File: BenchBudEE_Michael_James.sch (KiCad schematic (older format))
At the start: 0 parts

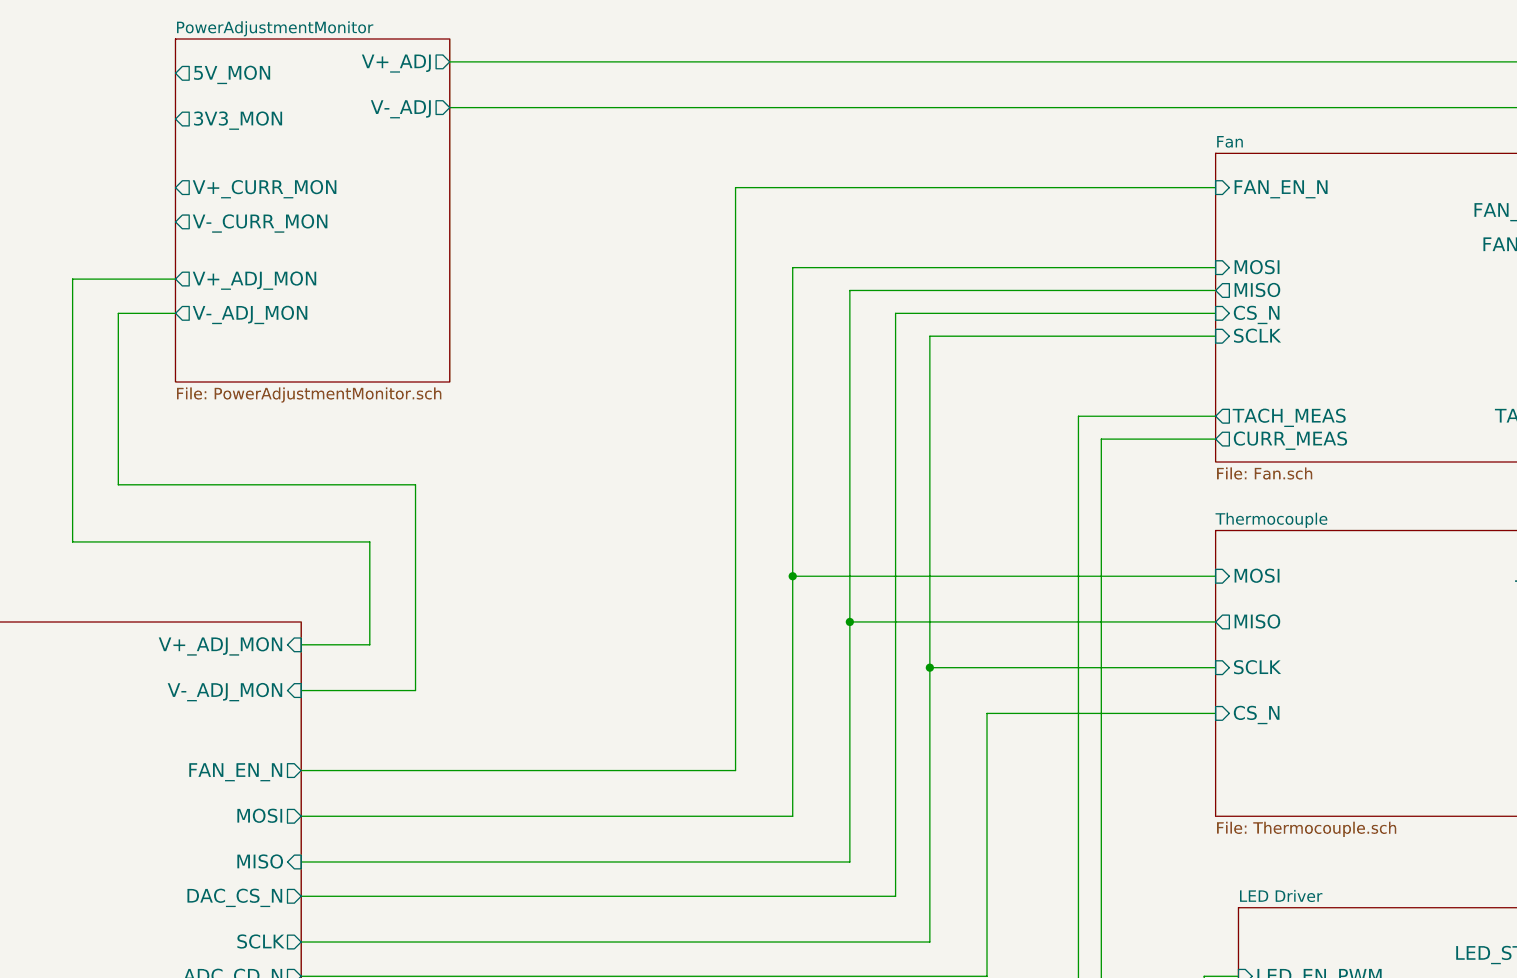
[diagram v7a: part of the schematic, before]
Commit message: M3 U9
Revisiting the Current/Fan Module
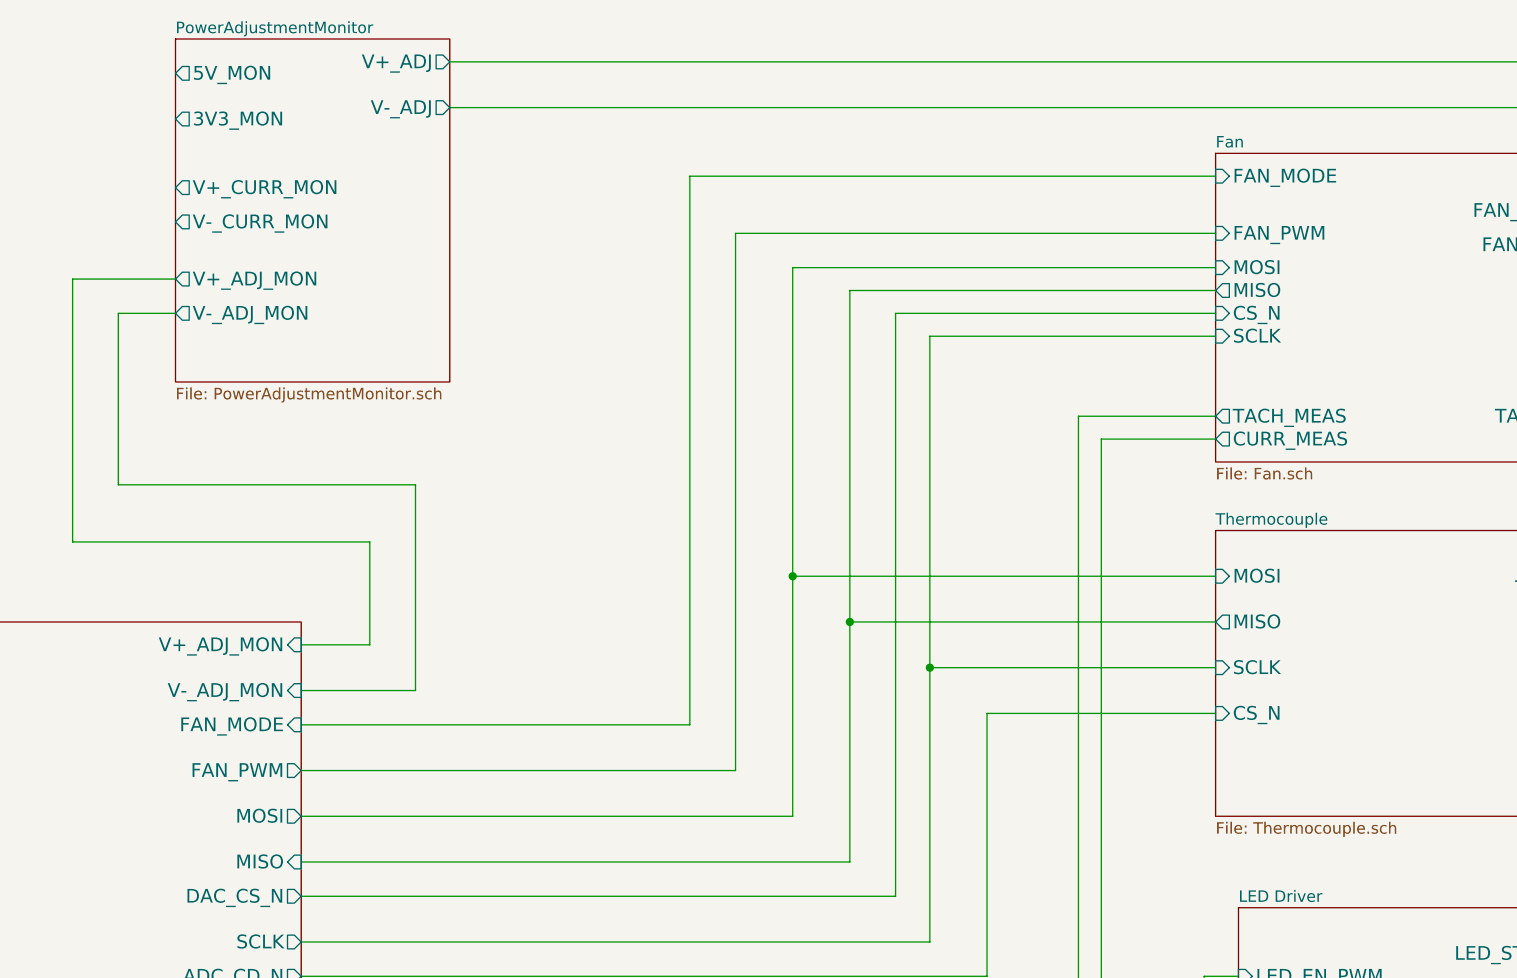
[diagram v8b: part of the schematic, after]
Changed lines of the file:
@@
 F6 "RELAY+" I R 4000 6500 60
 F7 "RELAY-" I R 4000 6800 60
-F8 "FAN_EN_N" O R 4000 3750 60
-F9 "CURR_MEAS" I R 4000 5300 60
-F10 "V+_ADJ_MON" I R 4000 3200 60
-F11 "V-_ADJ_MON" I R 4000 3400 60
-F12 "LED_EN_PWM" I R 4000 4950 60
-F13 "DAC_CS_N" O R 4000 4300 60
-F14 "ADC_CD_N" O R 4000 4650 60
+F8 "CURR_MEAS" I R 4000 5300 60
+F9 "V+_ADJ_MON" I R 4000 3200 60
+F10 "V-_ADJ_MON" I R 4000 3400 60
+F11 "LED_EN_PWM" I R 4000 4950 60
+F12 "DAC_CS_N" O R 4000 4300 60
+F13 "ADC_CD_N" O R 4000 4650 60
+F14 "FAN_PWM" O R 4000 3750 60
+F15 "FAN_MODE" I R 4000 3550 60
 $EndSheet
 $Sheet
@@
 F8 "TACH_IN" I R 9650 2200 60
 F9 "TACH_MEAS" O L 8000 2200 60
-F10 "FAN_EN_N" I L 8000 1200 60
-F11 "CURR_MEAS" O L 8000 2300 60
+F10 "CURR_MEAS" O L 8000 2300 60
+F11 "FAN_PWM" I L 8000 1400 60
+F12 "FAN_MODE" I L 8000 1150 60
 $EndSheet
 $Sheet
@@
 	4000 3750 5900 3750
 Wire Wire Line
-	5900 3750 5900 1200
-Wire Wire Line
-	5900 1200 8000 1200
-Wire Wire Line
-	4000 3950 6150 3950
-Wire Wire Line
-	6150 3950 6150 1550
+	5900 3750 5900 1400
+Wire Wire Line
+	5900 1400 8000 1400
+Wire Wire Line
+	6150 3950 4000 3950
+Wire Wire Line
+	6150 1550 6150 3950
 Wire Wire Line
 	6150 1550 8000 1550
@@
 Wire Wire Line
 	7500 5500 4000 5500
+Wire Wire Line
+	5700 1150 8000 1150
+Wire Wire Line
+	5700 3550 5700 1150
+Wire Wire Line
+	4000 3550 5700 3550
 $EndSCHEMATC
